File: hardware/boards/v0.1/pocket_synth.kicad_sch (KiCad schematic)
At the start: 6 parts

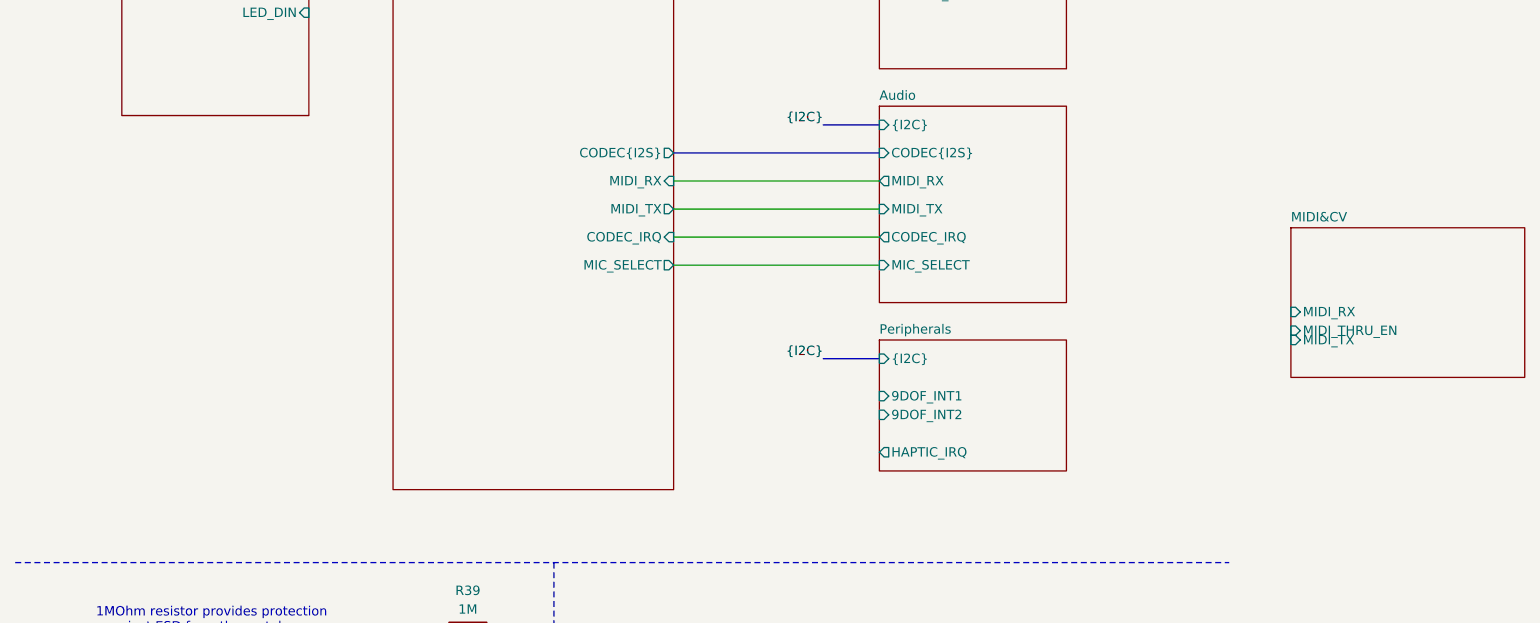
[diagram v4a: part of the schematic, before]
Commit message: feat: schematic organization, MIDI port routing
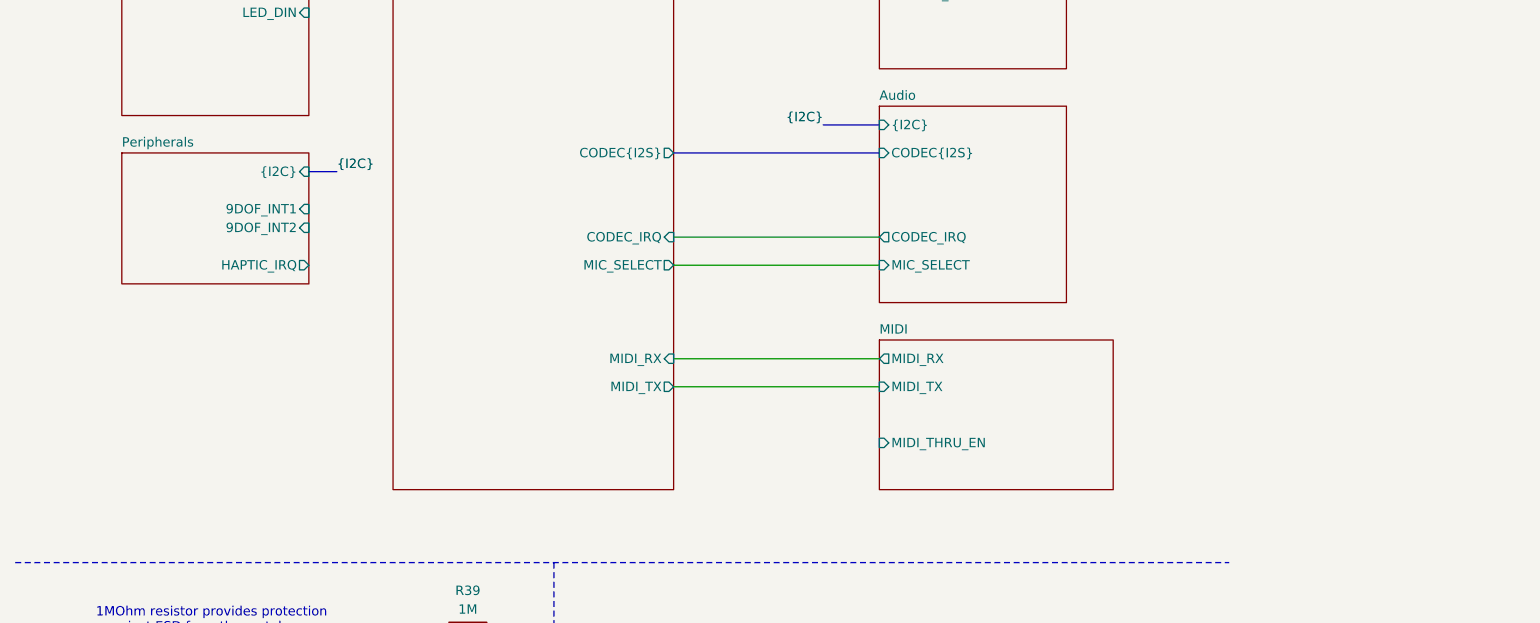
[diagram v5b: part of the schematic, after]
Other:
- sheet MIDI&CV renamed MIDI
- sheet Audio ports: added none; removed MIDI_RX, MIDI_TX
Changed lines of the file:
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@@
 	(bus
 		(pts
-			(xy 121.92 138.43) (xy 129.54 138.43)
+			(xy 55.88 113.03) (xy 52.07 113.03)
 		)
 		(stroke
@@
 	(wire
 		(pts
-			(xy 101.6 114.3) (xy 129.54 114.3)
+			(xy 101.6 138.43) (xy 129.54 138.43)
 		)
 		(stroke
@@
 	(wire
 		(pts
-			(xy 101.6 118.11) (xy 129.54 118.11)
+			(xy 101.6 142.24) (xy 129.54 142.24)
 		)
 		(stroke
@@
 	)
 	(label "{I2C}"
-		(at 121.92 138.43 180)
+		(at 55.88 113.03 0)
 		(effects
 			(font
@@
 				(thickness 0.1588)
 			)
-			(justify right bottom)
+			(justify left bottom)
 		)
 	)
@@
 			)
 		)
+		(property "Connector" ""
+			(at 19.05 182.88 0)
+			(effects
+				(font
+					(size 1.27 1.27)
+				)
+			)
+		)
 		(pin "1"
 		)
@@
 			)
 		)
+		(property "Connector" ""
+			(at 48.26 182.88 0)
+			(effects
+				(font
+					(size 1.27 1.27)
+				)
+			)
+		)
 		(pin "1"
 		)
@@
 			)
 		)
+		(property "Connector" ""
+			(at 29.21 182.88 0)
+			(effects
+				(font
+					(size 1.27 1.27)
+				)
+			)
+		)
 		(pin "1"
 		)
@@
 			)
 		)
+		(property "Connector" ""
+			(at 38.1 182.88 0)
+			(effects
+				(font
+					(size 1.27 1.27)
+				)
+			)
+		)
 		(pin "1"
 		)
@@
 			)
 		)
+		(property "Connector" ""
+			(at 73.66 175.26 0)
+			(effects
+				(font
+					(size 1.27 1.27)
+				)
+			)
+		)
 		(pin "2"
 		)
@@
 			)
 		)
+		(property "Connector" ""
+			(at 73.66 187.96 0)
+			(effects
+				(font
+					(size 1.27 1.27)
+				)
+			)
+		)
 		(pin "1"
 		)
@@
 		)
 		(pin "MIDI_RX" input
-			(at 101.6 114.3 0)
+			(at 101.6 138.43 0)
 			(effects
 				(font
@@
 		)
 		(pin "MIDI_TX" output
-			(at 101.6 118.11 0)
+			(at 101.6 142.24 0)
 			(effects
 				(font
@@
 	)
 	(sheet
-		(at 185.42 120.65)
+		(at 129.54 135.89)
 		(size 31.75 20.32)
 		(exclude_from_sim no)
@@
 			(color 0 0 0 0.0000)
 		)
-		(property "Sheetname" "MIDI&CV"
-			(at 185.42 119.9384 0)
+		(property "Sheetname" "MIDI"
+			(at 129.54 135.1784 0)
 			(effects
 				(font
@@
 		)
 		(property "Sheetfile" "midi_cv.kicad_sch"
-			(at 185.42 141.5546 0)
+			(at 129.54 156.7946 0)
 			(effects
 				(font
@@
 			)
 		)
-		(pin "MIDI_RX" input
-			(at 185.42 132.08 180)
+		(pin "MIDI_RX" output
+			(at 129.54 138.43 180)
 			(effects
 				(font
@@
 		)
 		(pin "MIDI_THRU_EN" input
-			(at 185.42 134.62 180)
+			(at 129.54 149.86 180)
 			(effects
 				(font
@@
 		)
 		(pin "MIDI_TX" input
-			(at 185.42 135.89 180)
+			(at 129.54 142.24 180)
 			(effects
 				(font
@@
 			)
 		)
-		(pin "MIDI_RX" output
-			(at 129.54 114.3 180)
-			(effects
-				(font
-					(size 1.27 1.27)
-				)
-				(justify left)
-			)
-		)
-		(pin "MIDI_TX" input
-			(at 129.54 118.11 180)
-			(effects
-				(font
-					(size 1.27 1.27)
-				)
-				(justify left)
-			)
-		)
 		(instances
 			(project "pocket_synth"
@@
 	)
 	(sheet
-		(at 129.54 135.89)
+		(at 26.67 110.49)
 		(size 25.4 17.78)
 		(exclude_from_sim no)
@@
 		)
 		(property "Sheetname" "Peripherals"
-			(at 129.54 135.1784 0)
+			(at 26.67 109.7784 0)
 			(effects
 				(font
@@
 		)
 		(property "Sheetfile" "peripherals.kicad_sch"
-			(at 129.54 154.2546 0)
+			(at 26.67 128.8546 0)
 			(effects
 				(font
@@
 		)
 		(pin "9DOF_INT1" input
-			(at 129.54 143.51 180)
-			(effects
-				(font
-					(size 1.27 1.27)
-				)
-				(justify left)
+			(at 52.07 118.11 0)
+			(effects
+				(font
+					(size 1.27 1.27)
+				)
+				(justify right)
 			)
 		)
 		(pin "9DOF_INT2" input
-			(at 129.54 146.05 180)
-			(effects
-				(font
-					(size 1.27 1.27)
-				)
-				(justify left)
+			(at 52.07 120.65 0)
+			(effects
+				(font
+					(size 1.27 1.27)
+				)
+				(justify right)
 			)
 		)
 		(pin "HAPTIC_IRQ" output
-			(at 129.54 151.13 180)
-			(effects
-				(font
-					(size 1.27 1.27)
-				)
-				(justify left)
+			(at 52.07 125.73 0)
+			(effects
+				(font
+					(size 1.27 1.27)
+				)
+				(justify right)
 			)
 		)
 		(pin "{I2C}" input
-			(at 129.54 138.43 180)
-			(effects
-				(font
-					(size 1.27 1.27)
-				)
-				(justify left)
-			)
-		)
+			(at 52.07 113.03 0)
+			(effects
+				(font
+					(size 1.27 1.27)
+				)
+				(justify right)
+			)
+		)

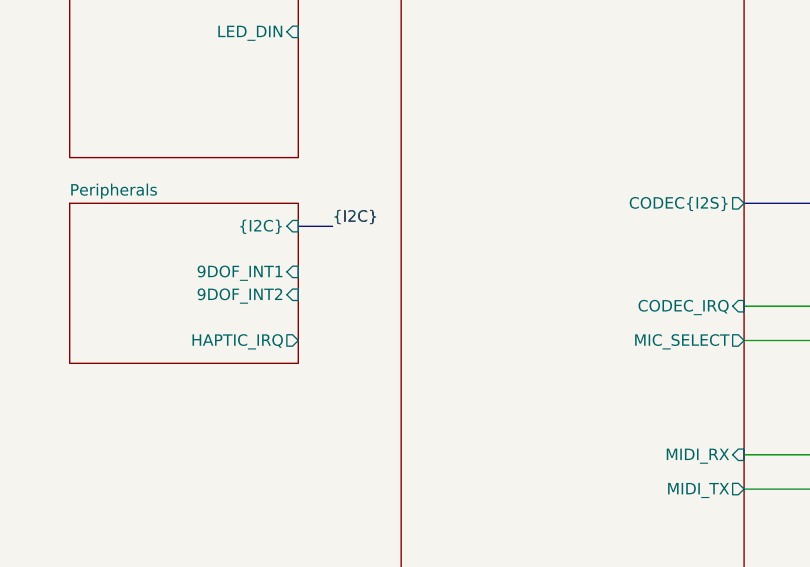
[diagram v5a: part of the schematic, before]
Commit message: feat: route audio components
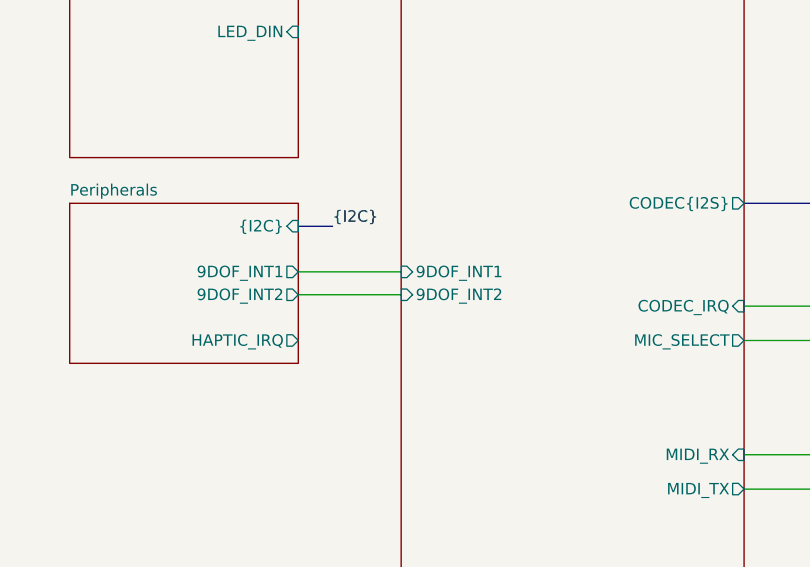
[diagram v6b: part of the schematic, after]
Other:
- sheet MCU ports: added 9DOF_INT1, 9DOF_INT2; removed none
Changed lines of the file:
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@@
+	(wire
+		(pts
+			(xy 52.07 118.11) (xy 63.5 118.11)
+		)
+		(stroke
+			(width 0)
+			(type default)
+		)
+	)
 	(wire
 		(pts
@@
 		(pts
 			(xy 22.86 38.1) (xy 26.67 38.1)
+		)
+		(stroke
+			(width 0)
+			(type default)
+		)
+	)
+	(wire
+		(pts
+			(xy 52.07 120.65) (xy 63.5 120.65)
 		)
 		(stroke
@@
 			)
 		)
+		(pin "9DOF_INT1" input
+			(at 63.5 118.11 180)
+			(effects
+				(font
+					(size 1.27 1.27)
+				)
+				(justify left)
+			)
+		)
+		(pin "9DOF_INT2" input
+			(at 63.5 120.65 180)
+			(effects
+				(font
+					(size 1.27 1.27)
+				)
+				(justify left)
+			)
+		)
 		(instances
 			(project "pocket_synth"
@@
 			)
 		)
-		(pin "9DOF_INT1" input
+		(pin "9DOF_INT1" output
 			(at 52.07 118.11 0)
 			(effects
@@
 			)
 		)
-		(pin "9DOF_INT2" input
+		(pin "9DOF_INT2" output
 			(at 52.07 120.65 0)
 			(effects

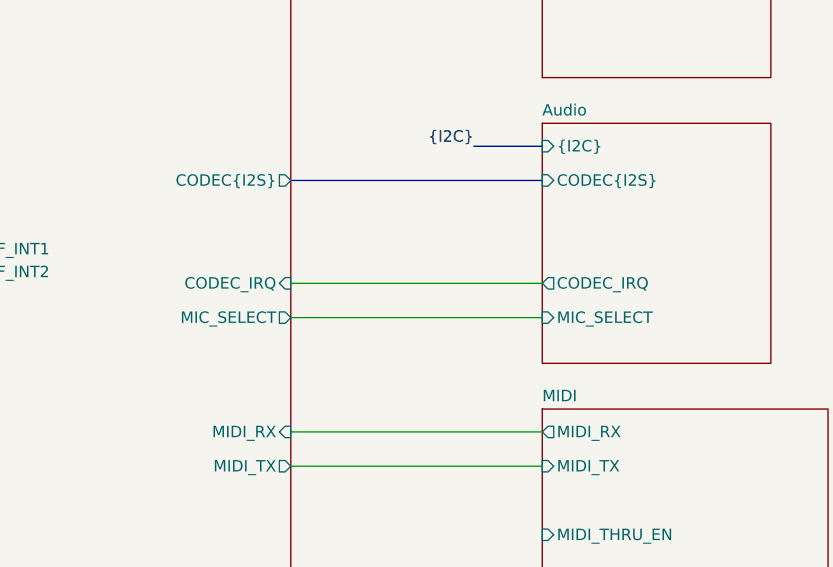
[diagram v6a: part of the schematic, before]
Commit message: feat: FM receiver routing
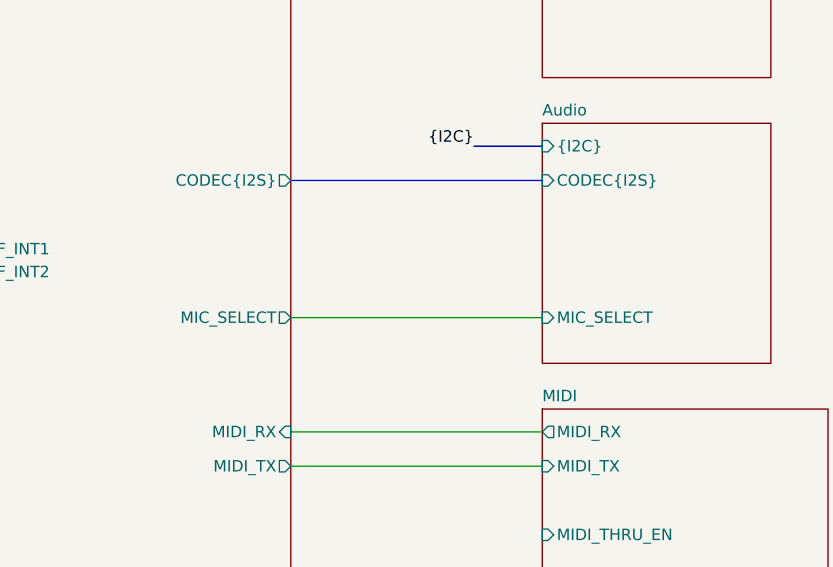
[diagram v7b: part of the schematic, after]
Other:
- sheet Audio ports: added none; removed CODEC_IRQ
- sheet MCU ports: added none; removed CODEC_IRQ
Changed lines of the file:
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@@
-	(wire
-		(pts
-			(xy 101.6 121.92) (xy 129.54 121.92)
-		)
-		(stroke
-			(width 0)
-			(type default)
-		)
-	)
 	(wire
 		(pts
@@
 			)
 		)
-		(pin "CODEC_IRQ" input
-			(at 101.6 121.92 0)
-			(effects
-				(font
-					(size 1.27 1.27)
-				)
-				(justify right)
-			)
-		)
 		(pin "{AUDIO_UART}" output
 			(at 63.5 64.77 180)
@@
 			(effects
 				(font
-					(size 1.27 1.27)
-				)
-				(justify left)
-			)
-		)
-		(pin "CODEC_IRQ" output
-			(at 129.54 121.92 180)
-			(effects
-				(font
